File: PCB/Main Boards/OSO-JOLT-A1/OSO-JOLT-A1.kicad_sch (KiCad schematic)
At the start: 34 parts, among them J1 OSO_SWD, J2 FH19C-9S-0.5SH_10_, Q1 Q_NMOS_GSD, U1 ATSAML22J18A-MUT, U4 MIC5365-3.3YC5-TR, X1 Crystal

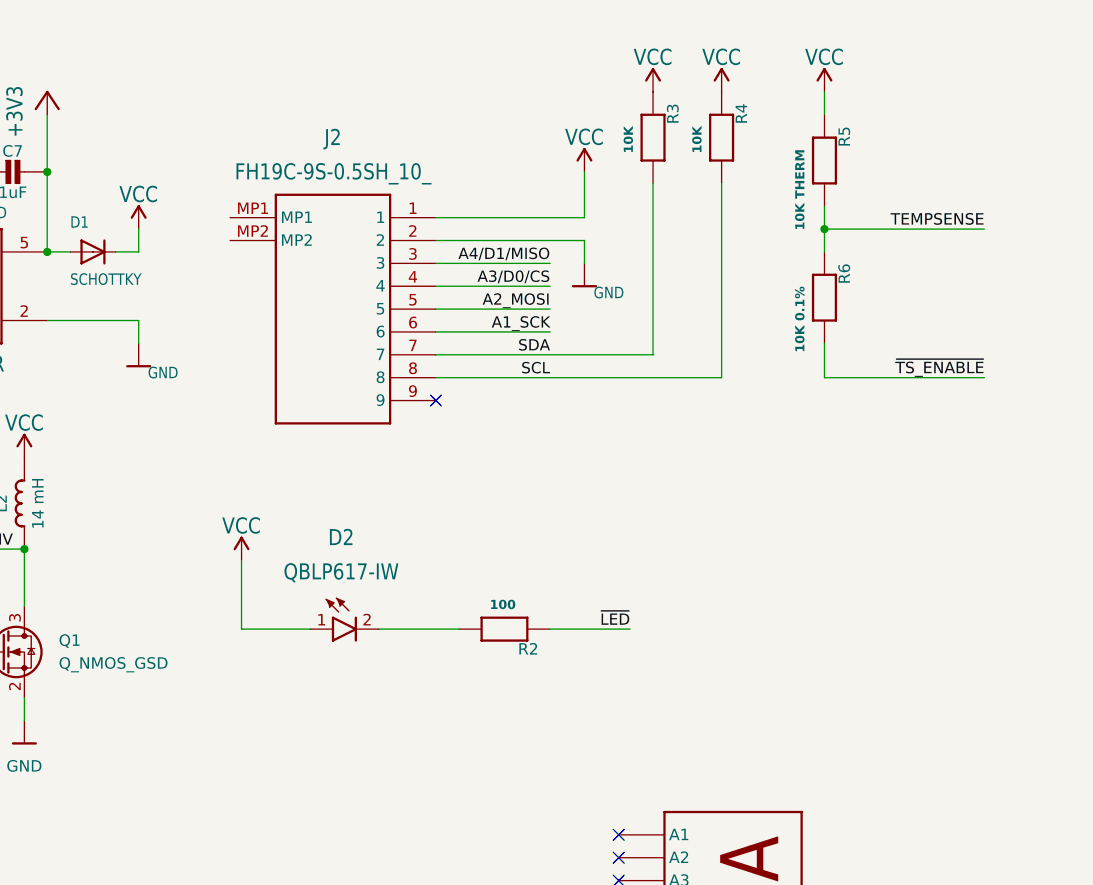
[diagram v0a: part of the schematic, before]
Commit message: Began adding accelerometer board directly on PCB
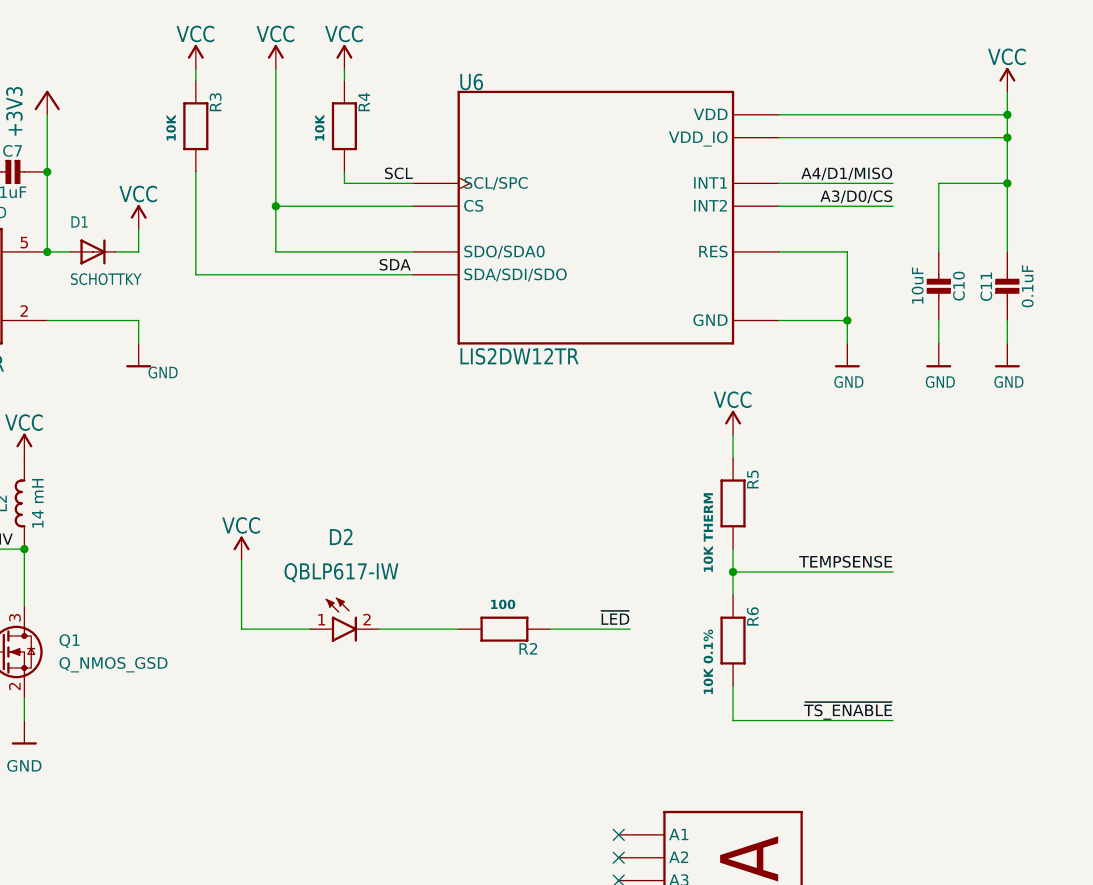
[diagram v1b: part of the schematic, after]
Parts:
- removed J2: FH19C-9S-0.5SH_10_, OSO-SWAT-A1-05:FH19C9S05SH10, symbol OSO-SWAT-A1-05-eagle-import:FH19C-9S-0.5SH_10_
- added C10: 10uF, OSO-MISC-21-021 Sensor Watch Motion II:_0603MP, symbol OSO-MISC-21-021 Sensor Watch Motion II-eagle-import:CAP_CERAMIC_0603MP
- added C11: 0.1uF, OSO-MISC-21-021 Sensor Watch Motion II:_0603MP, symbol OSO-MISC-21-021 Sensor Watch Motion II-eagle-import:CAP_CERAMIC_0603MP
- added U6: LIS2DW12TR, OSO-MISC-21-021 Sensor Watch Motion II:LGA12R50P4X4_200X200X70, symbol OSO-MISC-21-021 Sensor Watch Motion II-eagle-import:LIS2DW12TR
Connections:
- net A3/D0/CS: now also U6.11 (INT2)
- net A4/D1/MISO: now also U6.12 (INT1)
- net GND: now also C10.1, C11.2, U6.6 (GND), U6.7 (RES), U6.8 (GND)
- net SCL: now also U6.1 (SCL/SPC)
- net SDA: now also U6.4 (SDA/SDI/SDO)
- net VCC: now also C10.2, C11.1, U6.10 (VDD_IO), U6.2 (CS), U6.3 (SDO/SDA0), U6.9 (VDD)
- no-connect marks 9 -> 8
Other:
- moved on the sheet: R3, R4, R5, R6

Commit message: Revert "Began adding accelerometer board directly on PCB"
This reverts commit 8b1a0a982f9e72f020d5a62f3937e948766a17b7.
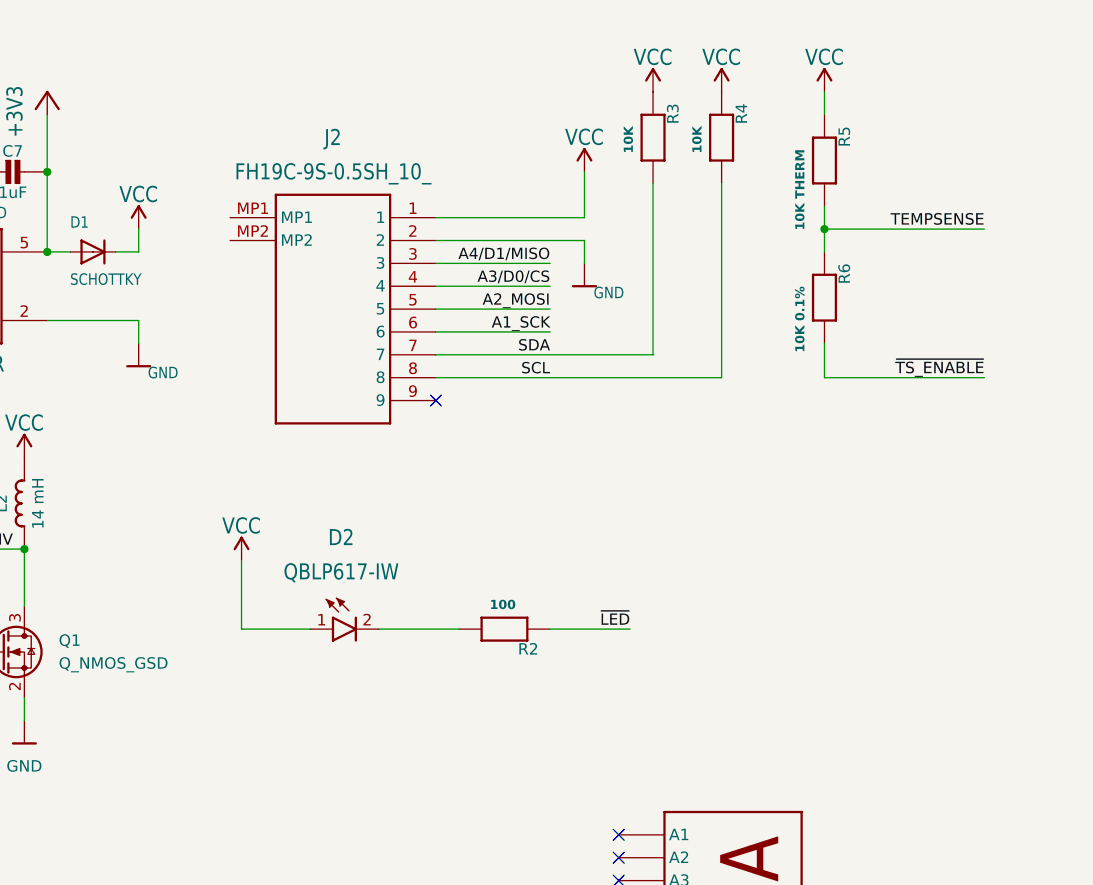
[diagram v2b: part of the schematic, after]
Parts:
- removed C10: 10uF, OSO-MISC-21-021 Sensor Watch Motion II:_0603MP, symbol OSO-MISC-21-021 Sensor Watch Motion II-eagle-import:CAP_CERAMIC_0603MP
- removed C11: 0.1uF, OSO-MISC-21-021 Sensor Watch Motion II:_0603MP, symbol OSO-MISC-21-021 Sensor Watch Motion II-eagle-import:CAP_CERAMIC_0603MP
- removed U6: LIS2DW12TR, OSO-MISC-21-021 Sensor Watch Motion II:LGA12R50P4X4_200X200X70, symbol OSO-MISC-21-021 Sensor Watch Motion II-eagle-import:LIS2DW12TR
- added J2: FH19C-9S-0.5SH_10_, OSO-SWAT-A1-05:FH19C9S05SH10, symbol OSO-SWAT-A1-05-eagle-import:FH19C-9S-0.5SH_10_
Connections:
- net A1_SCK: now also J2.6
- net A2_MOSI: now also J2.5
- net A3/D0/CS: now also J2.4
- net A4/D1/MISO: now also J2.3
- net GND: now also J2.2
- net SCL: now also J2.8
- net SDA: now also J2.7
- net VCC: now also J2.1
- no-connect marks 8 -> 9
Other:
- moved on the sheet: R3, R4, R5, R6
